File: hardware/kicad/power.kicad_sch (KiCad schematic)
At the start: 3 parts, among them J1 Phoenix_MSTBA_2,5/3-G-5,08, Q1 AO3415A

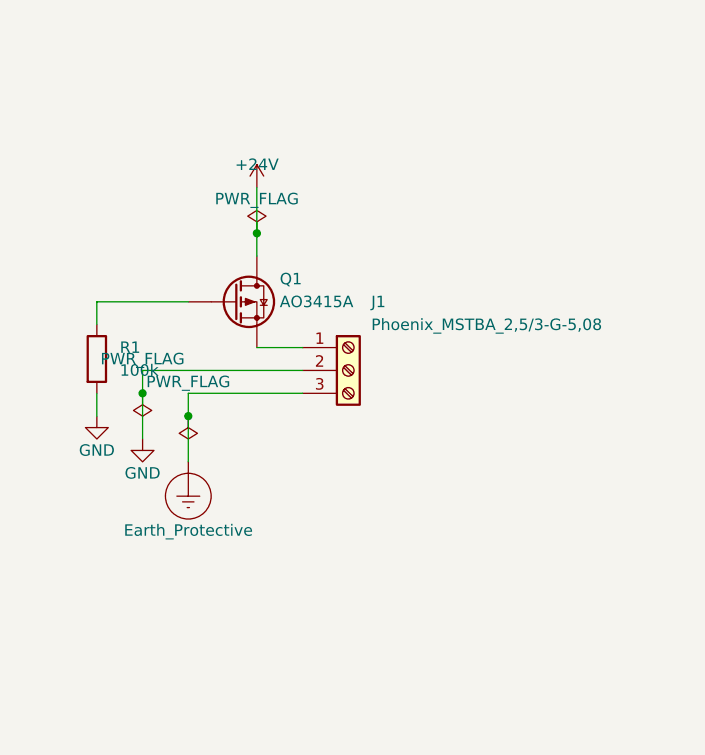
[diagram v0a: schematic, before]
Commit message: kicad: PTC fuse F1 + schematic render pipeline + power layout rework
Three bundled changes to the power-input section:

1. regenerate.py now exports every hierarchical sheet to
   renders/sch-<name>.{svg,png} via kicad-cli sch export svg.
   Gives reviewers and future agents a visual feedback loop
   for schematic edits, mirroring what we already have for
   PCB renders.

2. gen_power_sch() reworked: power flow is now left-to-right
   (J1 input on the left, protected +24V rail exiting to the
   right via Q1 and F1). Column spacing widened to ~15 mm
   between independent vertical wire columns. PWR_FLAG
   sentinels rotated 90 deg so their text labels sit beside
   the symbol rather than above, eliminating the value-text
   overlap with the adjacent power-flag symbols.

3. F1 polyfuse (PTC, 500 mA hold / 30 V) added in series on
   the +24V rail between Q1.drain and the +24V power flag.
   Provides resettable overcurrent protection - sized for
   ~200 mA average load, ~500 mA peak (WS2812 + radar + MCU
   + buck losses), trips around 1 A. Candidate parts: Bourns
   MF-MSMF050-2 or Littelfuse 1812L050PR (1812 SMD, verify
   JLCPCB Basic availability on order day).

ERC passes 0/0 across all 5 sheets. DRC unchanged 0/0.
Generation deterministic (bit-identical on consecutive runs).
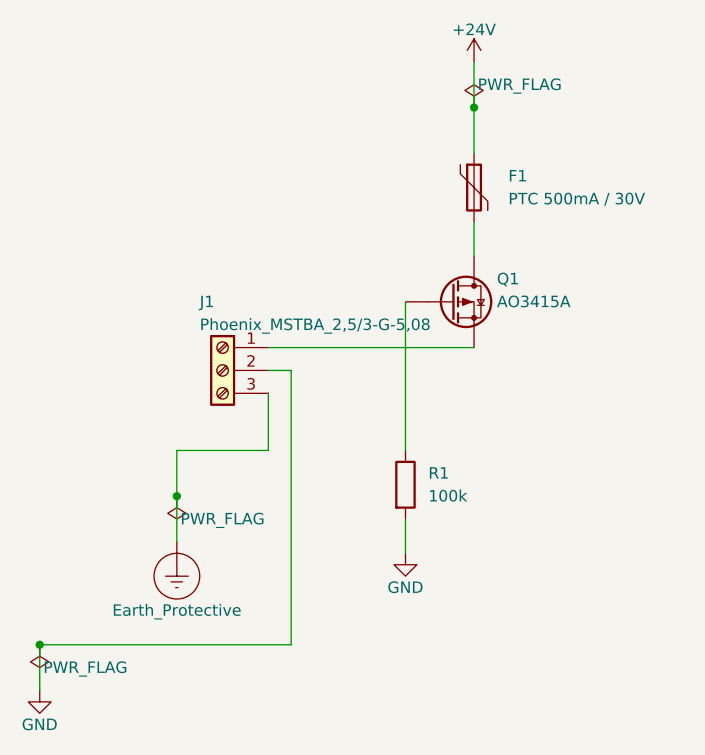
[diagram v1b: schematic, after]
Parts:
- added F1: PTC 500mA / 30V, symbol Device:Polyfuse
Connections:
- net +24V: now also F1.1; no longer Q1.D
- new net: F1.2, Q1.D

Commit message: kicad: TVS diode D1 (SMBJ24A) for surge protection on VIN
Adds unidirectional TVS diode D1 in parallel between the J1
pin 1 input (VIN, before Q1) and GND. Clamps transient
over-voltage events to ~38.9V at 1A peak surge, keeping the
downstream Q1 P-MOSFET (Vds_max = 40V) within its absolute
maximum rating.

SMBJ24A specifics:
- Vrwm 24V (does not conduct at the nominal 24V supply)
- Vbr 26.7V min (starts conducting above this)
- Vc 38.9V at 1A surge (sub-Q1-Vds_max with ~1.1V margin)
- 600W peak pulse power (10/1000 us)
- SMB (DO-214AA) package - JLCPCB Basic library candidate

Placement is BEFORE Q1 (not after) because Q1 itself needs
surge protection - a >40V transient on VIN would destroy Q1
before its reverse-polarity function could do anything
useful. F1 (PTC) downstream provides the second line of
defense, tripping on sustained over-current that would
follow a clamped over-voltage event.

ERC passes 0/0 across all 5 sheets. Generation deterministic.
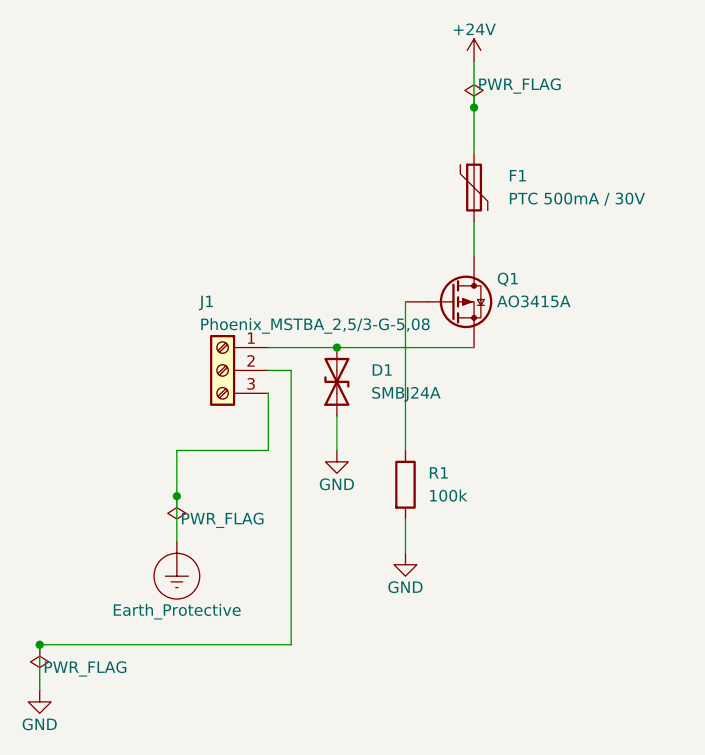
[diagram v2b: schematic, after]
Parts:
- added D1: SMBJ24A, symbol Device:D_TVS
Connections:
- net GND: now also D1.1 (A1)
- net at J1.1 (Pin_1), Q1.S: now also D1.2 (A2)
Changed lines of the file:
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@@
+(wire
+	(pts
+		(xy 100.33 101.6) (xy 100.33 105.41)
+	)
+	(stroke
+		(width 0)
+		(type default)
+	)
+)
 (wire
 	(pts
@@
 	(color 0 0 0 0)
 )
+(junction
+	(at 100.33 93.98)
+	(diameter 0)
+	(color 0 0 0 0)
+)
 (symbol
 	(lib_id "Connector:Screw_Terminal_01x03")
@@
 )
 (symbol
+	(lib_id "Device:D_TVS")
+	(at 100.33 97.79 90)
+	(unit 1)
+	(exclude_from_sim no)
+	(in_bom yes)
+	(on_board yes)
+	(dnp no)
+	(fields_autoplaced no)
+	(property "Reference" "D1"
+		(at 104.14 96.52 270)
+		(effects
+			(font
+				(size 1.27 1.27)
+			)
+			(justify left)
+		)
+	)
+	(property "Value" "SMBJ24A"
+		(at 104.14 99.06 270)
+		(effects
+			(font
+				(size 1.27 1.27)
+			)
+			(justify left)
+		)
+	)
+	(property "Footprint" ""
+		(at 100.33 97.79 0)
+		(effects
+			(font
+				(size 1.27 1.27)
+			)
+			(hide yes)
+		)
+	)
+	(property "Datasheet" ""
+		(at 100.33 97.79 0)
+		(effects
+			(font
+				(size 1.27 1.27)
+			)
+			(hide yes)
+		)
+	)
+	(property "Description" ""
+		(at 100.33 97.79 0)
+		(effects
+			(font
+				(size 1.27 1.27)
+			)
+			(hide yes)
+		)
+	)
+	(pin "1"
+	)
+	(pin "2"
+	)
+	(instances
+		(project "oas"
+			(path "/515343fe-5590-5fd9-97ec-5bed0f979de2/1557665b-a568-58fc-b40f-759ed4998499"
+				(reference "D1")
+				(unit 1)
+			)
+		)
+	)
+)
+(symbol
 	(lib_id "Device:Q_PMOS")
 	(at 113.03 88.9 0)
@@
 				(unit 1)
 			)
+		)
+	)
+)
+(symbol
+	(lib_id "power:GND")
+	(at 100.33 105.41 0)
+	(unit 1)
+	(exclude_from_sim no)
+	(in_bom yes)
+	(on_board yes)
+	(dnp no)
+	(fields_autoplaced yes)
+	(property "Reference" "#PWR05"
+		(at 100.33 101.6 0)
+		(effects
+			(font
+				(size 1.27 1.27)
+			)
+			(hide yes)
+		)
+	)
+	(property "Value" "GND"
+		(at 100.33 109.22 0)
+		(effects
+			(font
+				(size 1.27 1.27)
+			)
+		)
+	)
+	(property "Footprint" ""
+		(at 100.33 105.41 0)
+		(effects
+			(font
+				(size 1.27 1.27)
+			)
+			(hide yes)
+		)
+	)
+	(property "Datasheet" ""
+		(at 100.33 105.41 0)
+		(effects
+			(font
+				(size 1.27 1.27)
+			)
+			(hide yes)
+		)
+	)
+	(property "Description" ""
+		(at 100.33 105.41 0)
+		(effects
+			(font
+				(size 1.27 1.27)
+			)
+			(hide yes)
+		)
+	)
+	(pin "1"
+	)
+	(instances
+		(project "oas"
+			(path "/515343fe-5590-5fd9-97ec-5bed0f979de2/1557665b-a568-58fc-b40f-759ed4998499"
+				(reference "#PWR05")
+				(unit 1)
+			)
